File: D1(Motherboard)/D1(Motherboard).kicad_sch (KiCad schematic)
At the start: 50 parts, among them J1 WR-FPC_0.5mm_ZIF_V, J2 USB_C_Receptacle_USB2.0, J3 B2B-PH-K-S, Q1 NX2301P.215, SW1 CHS-02A, U1 CP2102N-A01-GQFN28, U2 ICM-20602, U3 WR-FPC_0.5mm_ZIF_H, U4 MIC5353-3.3YMT, U5 FAN5331SX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

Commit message: Test Commit for CADLAB
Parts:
- removed C20: 4.7u, Capacitor_SMD:C_0603_1608Metric, symbol Device:C_Small
- removed J2: USB_C_Receptacle_USB2.0, Connector_USB:USB_C_Receptacle_JAE_DX07S024WJ3R400, symbol Connector:USB_C_Receptacle_USB2.0
- added C?: 4.7u, Capacitor_SMD:C_0603_1608Metric, symbol Device:C_Small
- added J?: USB_C_Receptacle_USB2.0, Connector_USB:USB_C_Receptacle_JAE_DX07S024WJ3R400, symbol Connector:USB_C_Receptacle_USB2.0
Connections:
- net D+: now also J?.A6 (D+), J?.B6 (D+)
- net D-: now also J?.A7 (D-), J?.B7 (D-)
- net GND: now also C?.1, J?.A1 (GND), J?.A12 (GND), J?.B1 (GND), J?.B12 (GND)
- net VBUS: now also R?.2, U1.6 (VDD), C?.2, J?.A4 (VBUS), J?.A9 (VBUS), J?.B4 (VBUS), J?.B9 (VBUS)
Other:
- moved on the sheet: R?, U1

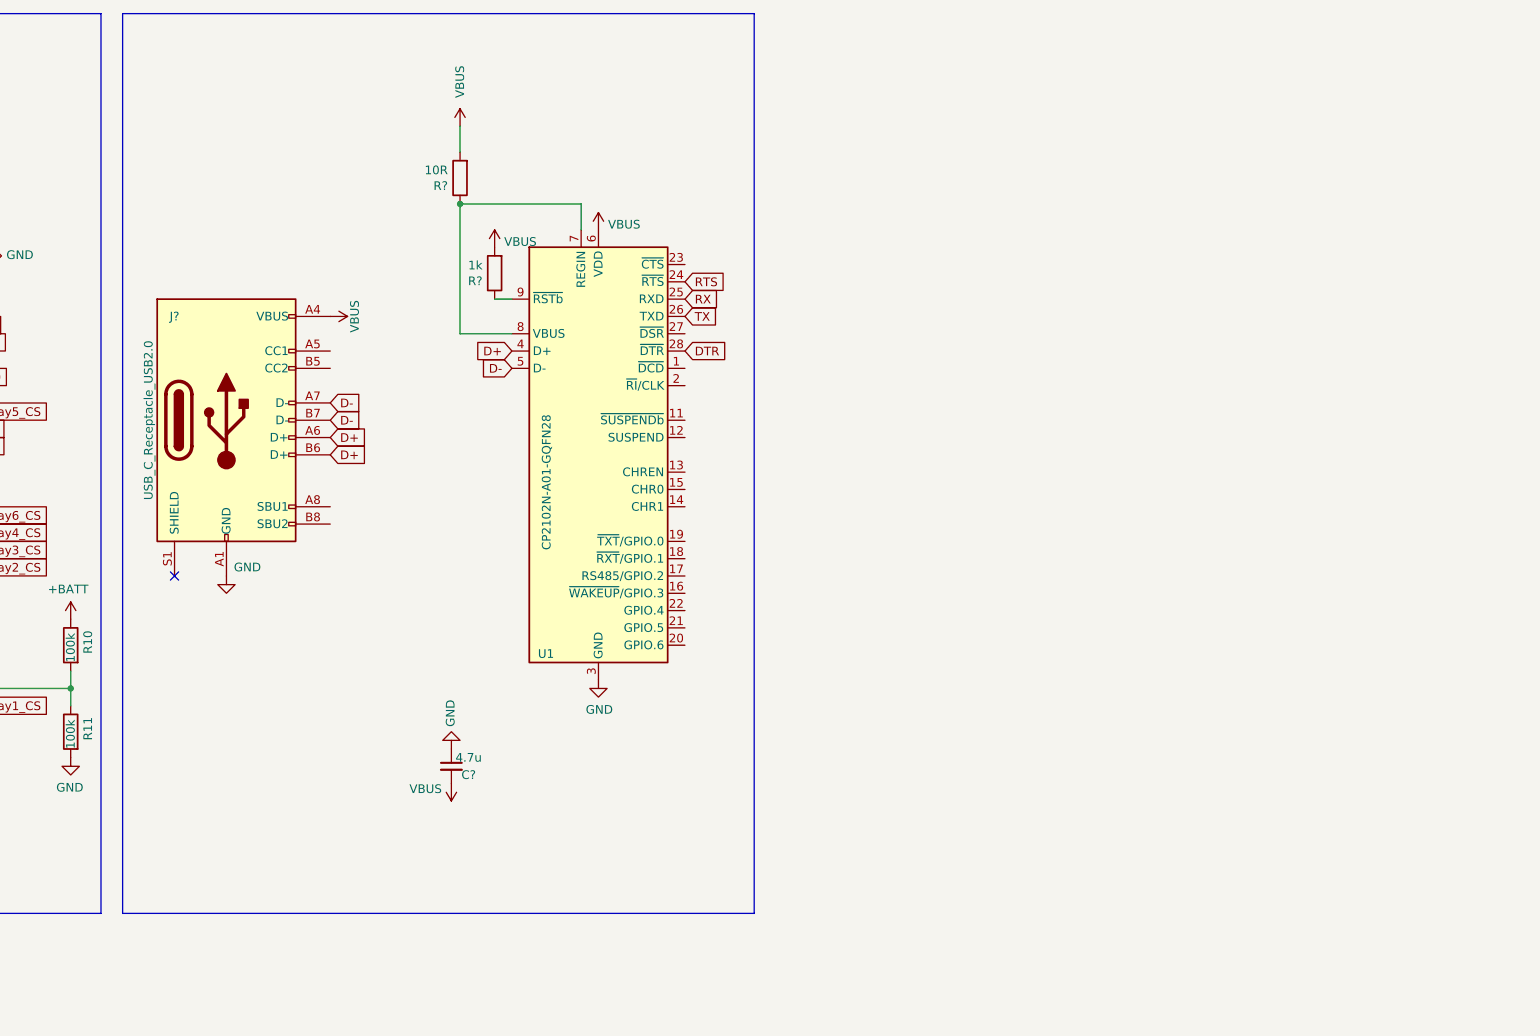
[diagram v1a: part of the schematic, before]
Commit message: Changed to KiCAD 6
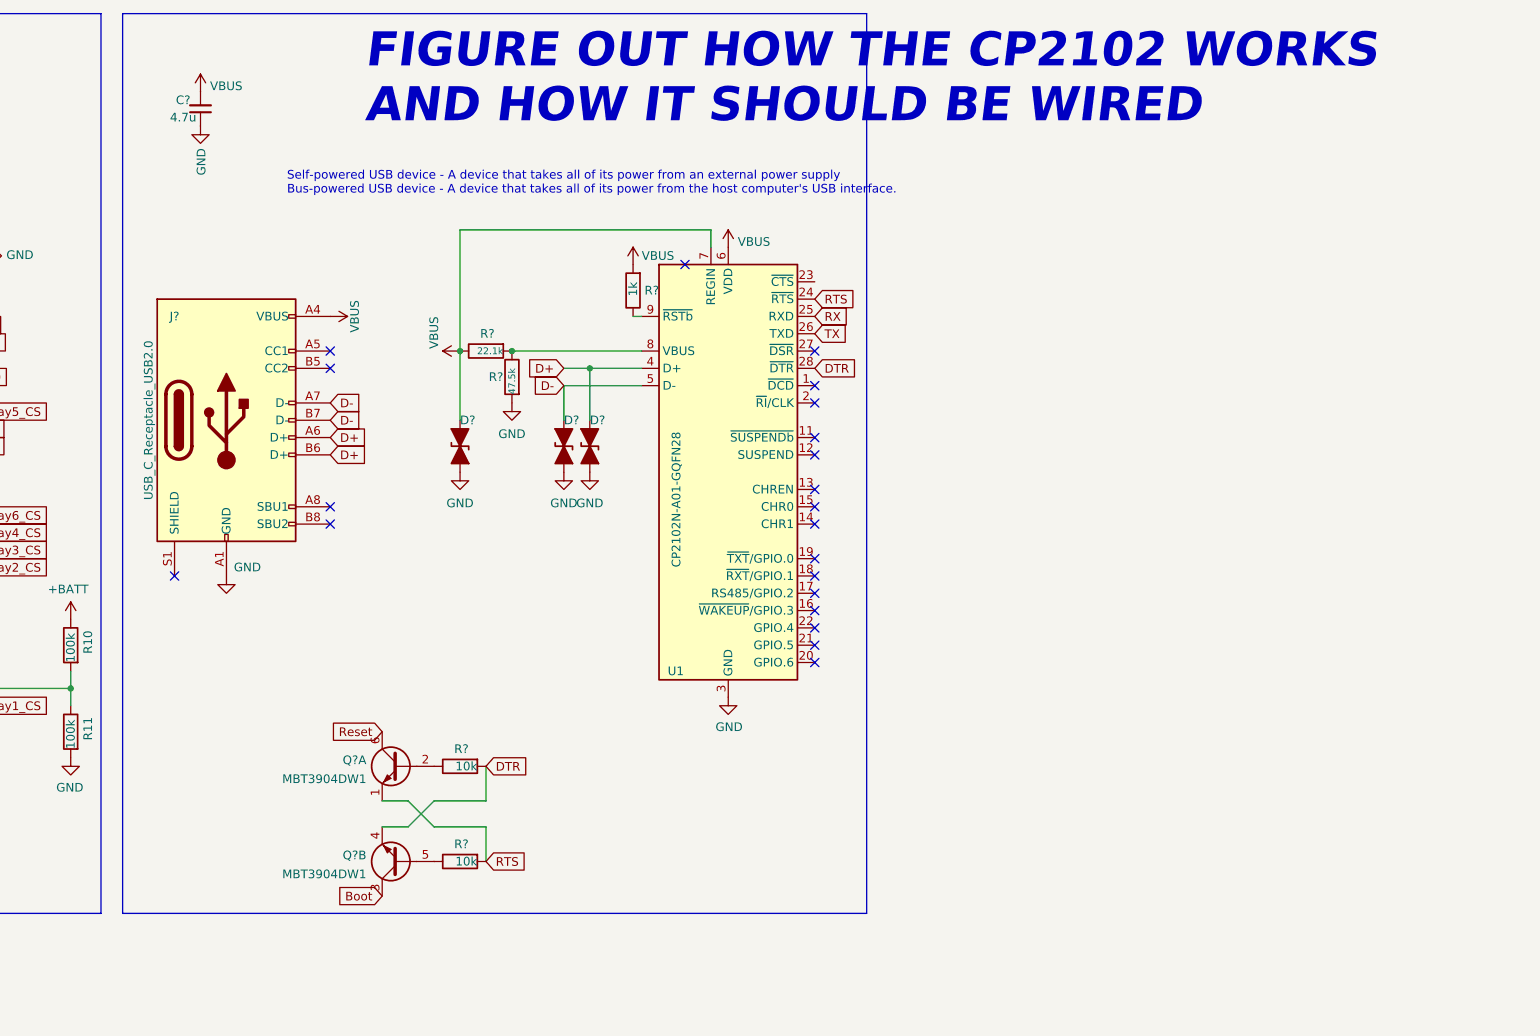
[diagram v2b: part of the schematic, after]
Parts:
- removed R?: 10R, Resistor_SMD:R_0603_1608Metric, symbol Device:R
- added D? (x3): ESD5B5.0S, Diode_SMD:D_SOD-523, symbol Device:D_TVS_ALT
- added Q? (x2): MBT3904DW1, Package_TO_SOT_SMD:SOT-363_SC-70-6, symbol Transistor_BJT:MBT3904DW1
- added R? (x2): 10k, Resistor_SMD:R_0603_1608Metric, symbol Device:R
- added R?: 22.1k, Resistor_SMD:R_0603_1608Metric, symbol Device:R
- added R?: 47.5k, Resistor_SMD:R_0603_1608Metric, symbol Device:R
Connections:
- net Boot: now also Q?.3 (C2)
- net D+: now also D?.2 (A2)
- net D-: now also D?.2 (A2)
- net DTR: now also Q?.4 (E2), R?.2
- net GND: now also D?.1 (A1), D?.1 (A1), D?.1 (A1), R?.2
- net RTS: now also Q?.1 (E1), R?.2
- net Reset: now also Q?.6 (C1)
- net VBUS: now also U1.7 (REGIN), D?.2 (A2), R?.1
- net at U1.8 (VBUS): now also R?.1, R?.2; no longer U1.7 (REGIN)
- new net: Q?.5 (B2), R?.1
- new net: Q?.2 (B1), R?.1
- no-connect marks 21 -> 41
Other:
- note added: "FIGURE OUT HOW THE CP2102 WORKS AND HOW IT SHOULD BE WIRED"
- note added: "Self-powered USB device - A device that takes all of its power from an external power supply Bus-powered USB device - A device that takes all of its power from the host computer's USB interface."
- moved on the sheet: C?, R?, U1

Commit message: Upload New Version from USB
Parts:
- gave numbers to parts that had none: 11

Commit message: Cleaned a bit more
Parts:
- D3: footprint LED_SMD:LED_0603_1608Metric_Castellated -> LED_SMD:LED_0603_1608Metric
- J2: footprint Connector_USB:USB_C_Receptacle_JAE_DX07S024WJ3R400 -> D1(Motherboard):GCT_USB4120-03-C
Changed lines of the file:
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@@
     (property "Reference" "D3" (id 0) (at 41.275 184.15 0))
     (property "Value" "GREEN" (id 1) (at 41.0972 178.4096 0))
-    (property "Footprint" "LED_SMD:LED_0603_1608Metric_Castellated" (id 2) (at 41.275 181.61 0)
+    (property "Footprint" "LED_SMD:LED_0603_1608Metric" (id 2) (at 41.275 181.61 0)
       (effects (font (size 1.27 1.27)) hide)
     )
@@
     (property "Reference" "J2" (id 0) (at 313.69 111.76 0))
     (property "Value" "USB_C_Receptacle_USB2.0" (id 1) (at 309.88 127 90))
-    (property "Footprint" "Connector_USB:USB_C_Receptacle_JAE_DX07S024WJ3R400" (id 2) (at 325.12 127 0)
+    (property "Footprint" "D1(Motherboard):GCT_USB4120-03-C" (id 2) (at 325.12 127 0)
       (effects (font (size 1.27 1.27)) hide)
     )
@@
     )
     (path "/00000000-0000-0000-0000-00006126d89d"
-      (reference "D3") (unit 1) (value "GREEN") (footprint "LED_SMD:LED_0603_1608Metric_Castellated")
+      (reference "D3") (unit 1) (value "GREEN") (footprint "LED_SMD:LED_0603_1608Metric")
     )
     (path "/00000000-0000-0000-0000-00006132caea"
@@
     )
     (path "/a0139dbf-800f-4b31-affb-7aba7e231628"
-      (reference "J2") (unit 1) (value "USB_C_Receptacle_USB2.0") (footprint "Connector_USB:USB_C_Receptacle_JAE_DX07S024WJ3R400")
+      (reference "J2") (unit 1) (value "USB_C_Receptacle_USB2.0") (footprint "D1(Motherboard):GCT_USB4120-03-C")
     )
     (path "/00000000-0000-0000-0000-000061240a63"

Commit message: Added ESP32 Datasheets to recources, started cleaning up layout for esp32
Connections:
- no-connect marks 41 -> 40
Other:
- note added: "CHECK THE CHIP FOR ESP32 AND THE FOOTPRINT"
- note added: "DOUBLE CHECK Autoprogram is the same as one on ESP32 Devboard, where the buttons dont interfere with the autoprogramming from the usb"
- note added: "DOUBLE CHECK DISPLAY CONNECTOR/BOARD CONNECTORS ARE CORRECT"
- note added: "FIND ANTENNA"
- note added: "FIND VALUES OF CAPS INDUCTORS FOR CRYSTAL AND ANTENNA"
- note removed: "ADD AUTO FLASH FEATURE"
- moved on the sheet: C1, C12, C13, C14, C15, C16, C17, C18, C19, C2, C20, C3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

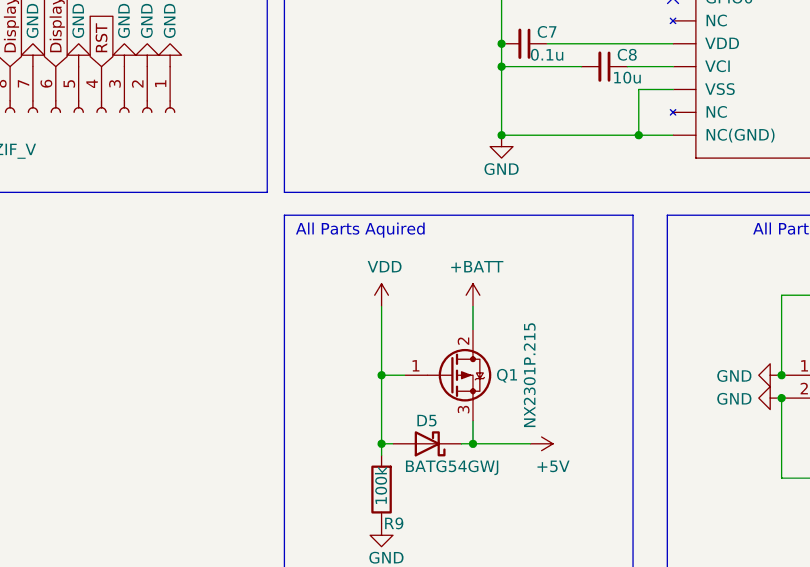
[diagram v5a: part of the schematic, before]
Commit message: Changed VDD to VBUS to match other references
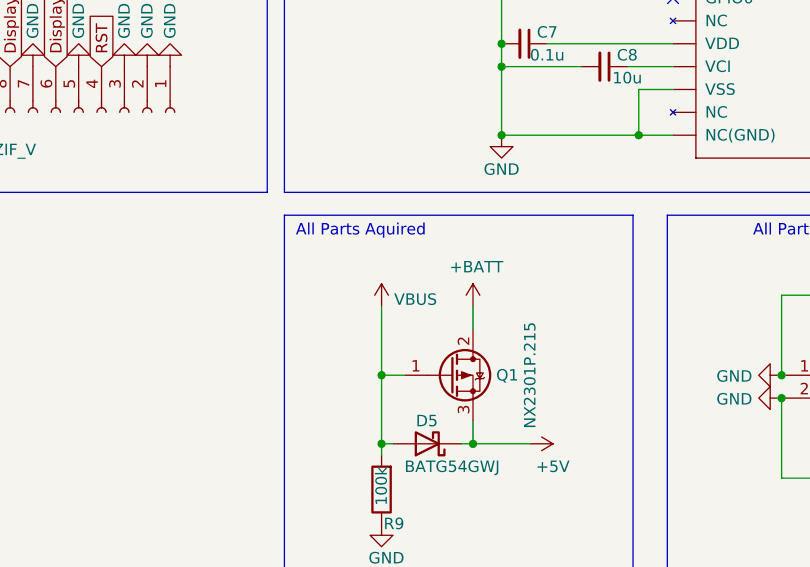
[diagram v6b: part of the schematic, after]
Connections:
- net VDD is gone; now on net VBUS: D5.2 (A), Q1.1 (G), R9.2
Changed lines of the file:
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@@
-    (pin "1")
-  )
-  (symbol (lib_id "power:VDD") (at 167.64 170.18 0) (unit 1)
-    (in_bom yes) (on_board yes)
-    (property "Reference" "#PWR0156" (id 0) (at 167.64 173.99 0)
-      (effects (font (size 1.27 1.27)) hide)
-    )
-    (property "Value" "VDD" (id 1) (at 168.021 165.7858 0))
-    (property "Footprint" "" (id 2) (at 167.64 170.18 0)
-      (effects (font (size 1.27 1.27)) hide)
-    )
-    (property "Datasheet" "" (id 3) (at 167.64 170.18 0)
-      (effects (font (size 1.27 1.27)) hide)
-    )
     (pin "1")
   )
@@
     (pin "S1")
   )
+  (symbol (lib_id "power:VBUS") (at 167.64 170.18 0) (unit 1)
+    (in_bom yes) (on_board yes) (fields_autoplaced)
+    (property "Reference" "#PWR?" (id 0) (at 167.64 173.99 0)
+      (effects (font (size 1.27 1.27)) hide)
+    )
+    (property "Value" "VBUS" (id 1) (at 169.037 169.389 0)
+      (effects (font (size 1.27 1.27)) (justify left))
+    )
+    (property "Footprint" "" (id 2) (at 167.64 170.18 0)
+      (effects (font (size 1.27 1.27)) hide)
+    )
+    (property "Datasheet" "" (id 3) (at 167.64 170.18 0)
+      (effects (font (size 1.27 1.27)) hide)
+    )
+    (pin "1")
+  )
   (symbol (lib_id "Device:R") (at 353.06 148.59 90) (mirror x) (unit 1)
     (in_bom yes) (on_board yes)
@@
       (reference "#PWR0155") (unit 1) (value "GND") (footprint "")
     )
-    (path "/00000000-0000-0000-0000-0000618789f5"
-      (reference "#PWR0156") (unit 1) (value "VDD") (footprint "")
-    )
     (path "/00000000-0000-0000-0000-0000618789fb"
       (reference "#PWR0157") (unit 1) (value "+BATT") (footprint "")
@@
       (reference "#PWR0166") (unit 1) (value "VBUS") (footprint "")
     )
+    (path "/bc3cf1c9-21e5-41ac-a860-04a6c449dfac"
+      (reference "#PWR?") (unit 1) (value "VBUS") (footprint "")
+    )
     (path "/00000000-0000-0000-0000-000061233b33"

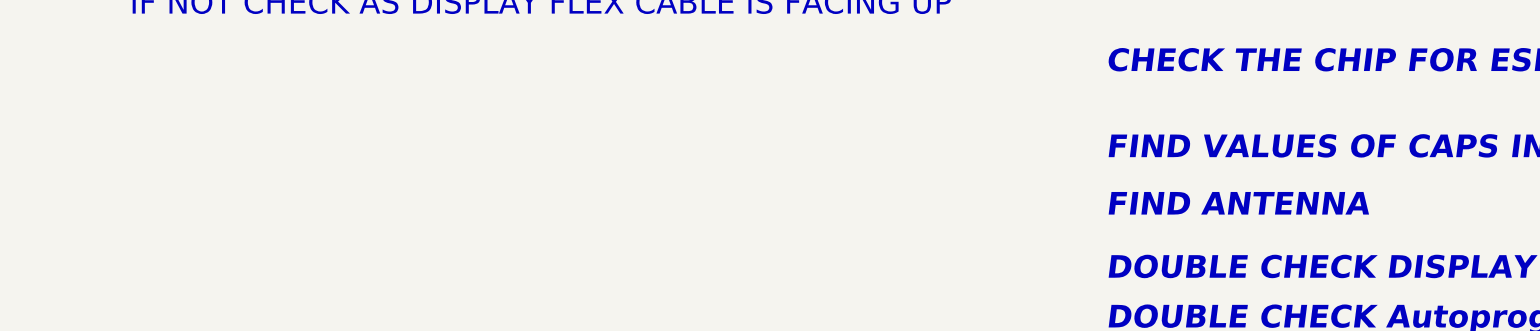
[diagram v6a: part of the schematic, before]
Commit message: Small update moving load sharing circuit, need to check voltage references
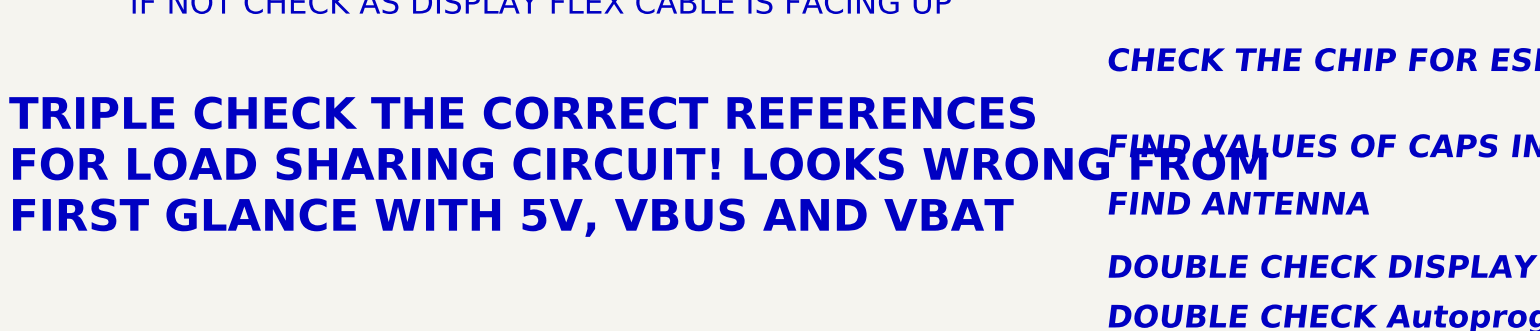
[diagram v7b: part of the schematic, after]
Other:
- note added: "TRIPLE CHECK THE CORRECT REFERENCES FOR LOAD SHARING CIRCUIT! LOOKS WRONG FROM FIRST GLANCE WITH 5V, VBUS AND VBAT"
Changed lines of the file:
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@@
     (effects (font (size 5 5) (thickness 1) bold italic) (justify left bottom))
+  )
+  (text "TRIPLE CHECK THE CORRECT REFERENCES\nFOR LOAD SHARING CIRCUIT! LOOKS WRONG FROM\nFIRST GLANCE WITH 5V, VBUS AND VBAT"
+    (at -17.78 267.97 0)
+    (effects (font (size 7 7) (thickness 1) bold) (justify left bottom))
   )
   (text "DOUBLE CHECK DISPLAY CONNECTOR/BOARD CONNECTORS ARE CORRECT"
@@
   (symbol (lib_id "power:VBUS") (at 167.64 170.18 0) (unit 1)
     (in_bom yes) (on_board yes) (fields_autoplaced)
-    (property "Reference" "#PWR?" (id 0) (at 167.64 173.99 0)
+    (property "Reference" "#PWR0156" (id 0) (at 167.64 173.99 0)
       (effects (font (size 1.27 1.27)) hide)
     )
@@
       (reference "#PWR0155") (unit 1) (value "GND") (footprint "")
     )
+    (path "/bc3cf1c9-21e5-41ac-a860-04a6c449dfac"
+      (reference "#PWR0156") (unit 1) (value "VBUS") (footprint "")
+    )
     (path "/00000000-0000-0000-0000-0000618789fb"
       (reference "#PWR0157") (unit 1) (value "+BATT") (footprint "")
@@
       (reference "#PWR0166") (unit 1) (value "VBUS") (footprint "")
     )
-    (path "/bc3cf1c9-21e5-41ac-a860-04a6c449dfac"
-      (reference "#PWR?") (unit 1) (value "VBUS") (footprint "")
-    )
     (path "/00000000-0000-0000-0000-000061233b33"
